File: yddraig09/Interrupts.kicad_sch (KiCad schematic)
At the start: 13 parts, among them U18 74LS32, U19 74LS574, U20 74LS32, U21 74LS11, U22 74LS147, U23 74LS540

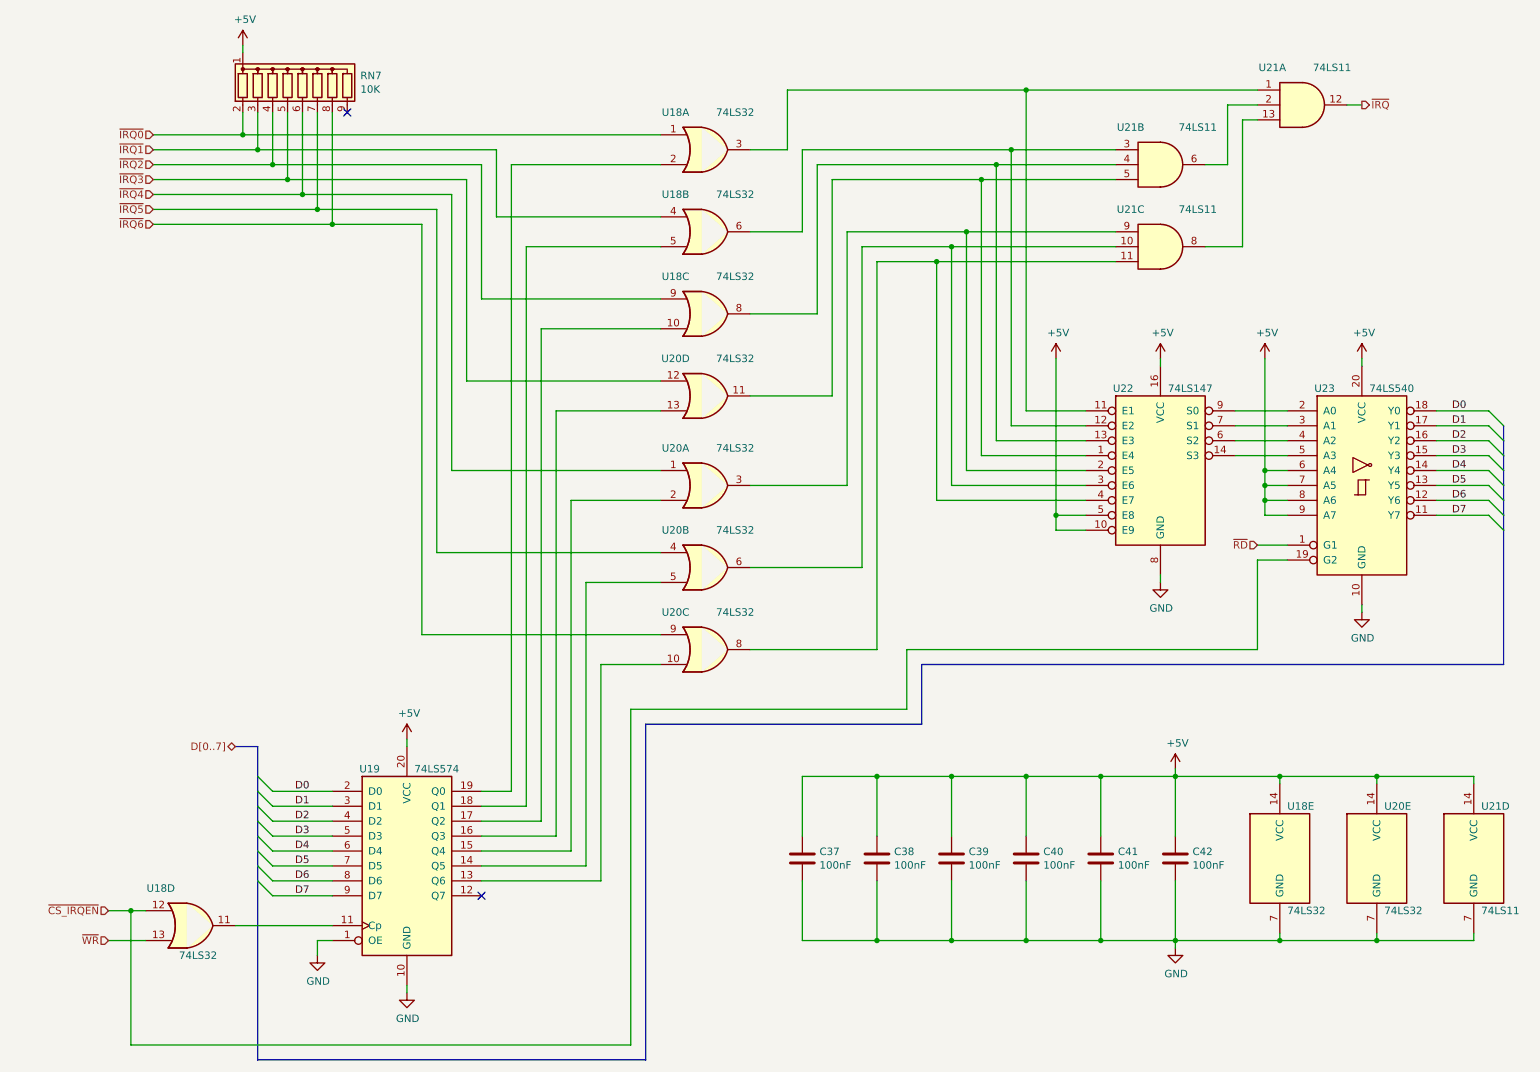
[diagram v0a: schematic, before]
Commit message: Finished changes to 6809 schematics
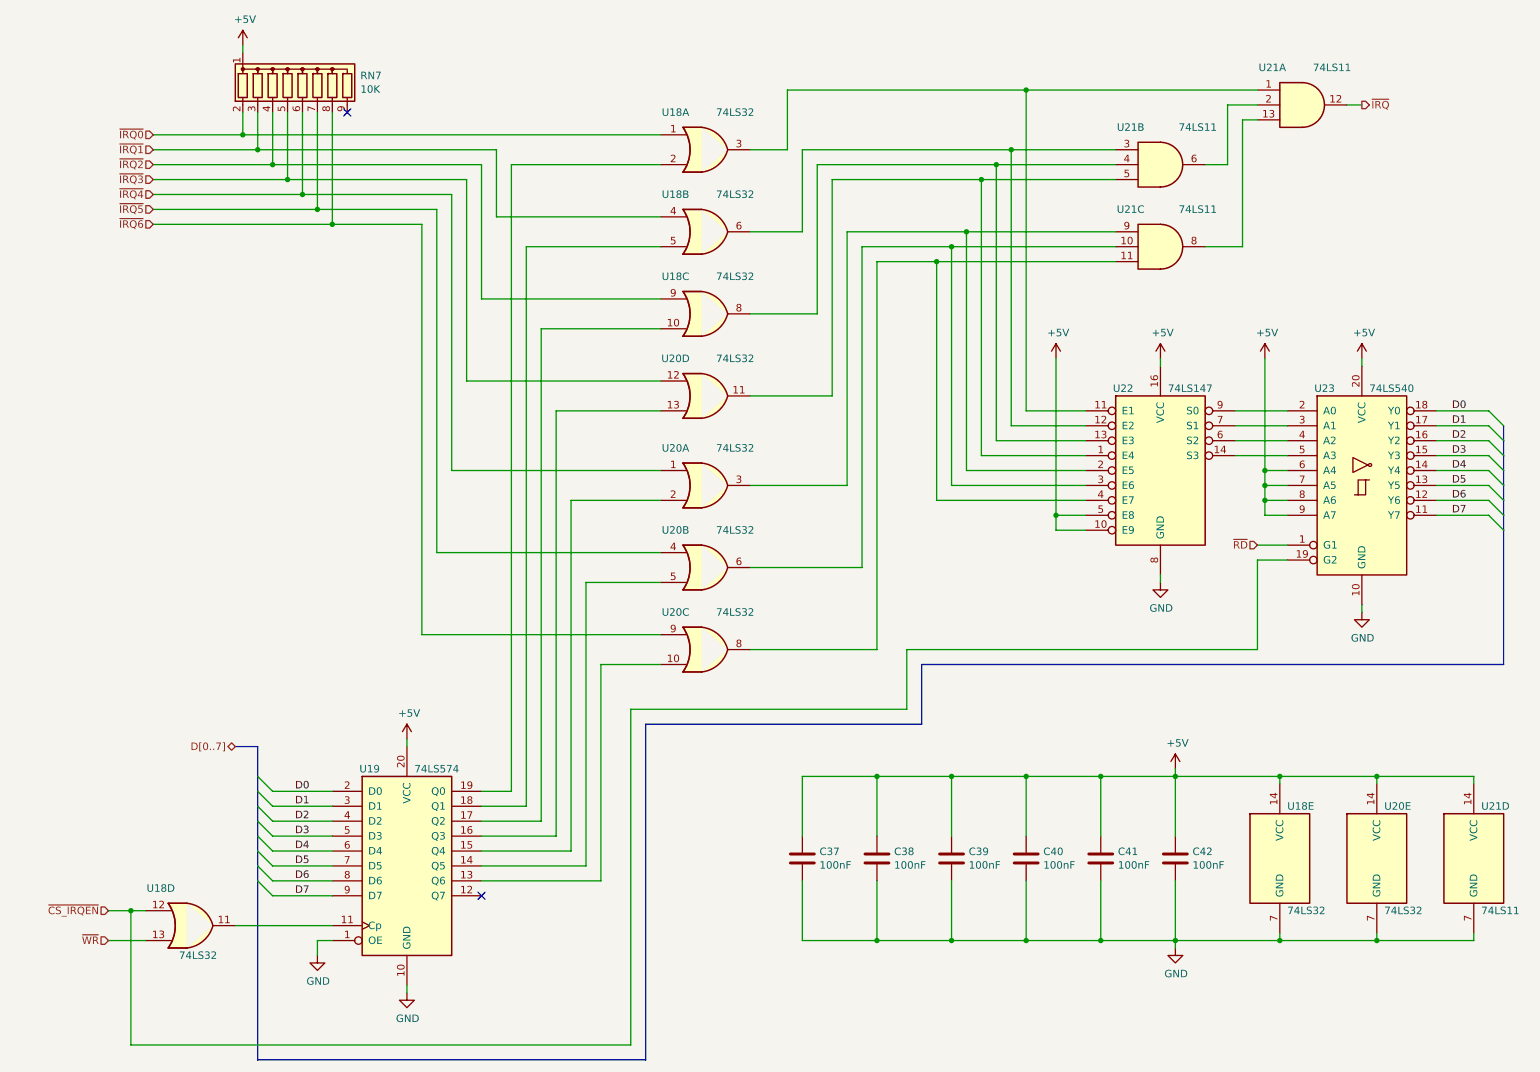
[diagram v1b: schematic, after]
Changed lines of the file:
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@@
 			)
 		)
-		(property "Description" ""
+		(property "Description" "Triple 3-input AND"
 			(at 241.3 30.48 0)
 			(effects
@@
 			)
 		)
-		(property "Description" ""
+		(property "Description" "Triple 3-input AND"
 			(at 217.17 40.64 0)
 			(effects
@@
 			)
 		)
-		(property "Description" ""
+		(property "Description" "Triple 3-input AND"
 			(at 217.17 54.61 0)
 			(effects
@@
 			)
 		)
-		(property "Description" ""
+		(property "Description" "Triple 3-input AND"
 			(at 270.51 158.75 0)
 			(effects
@@
 			)
 		)
-		(property "Description" ""
+		(property "Description" "Quad 2-input OR"
 			(at 139.7 38.1 0)
 			(effects
@@
 			)
 		)
-		(property "Description" ""
+		(property "Description" "Quad 2-input OR"
 			(at 139.7 52.07 0)
 			(effects
@@
 			)
 		)
-		(property "Description" ""
+		(property "Description" "Quad 2-input OR"
 			(at 139.7 66.04 0)
 			(effects
@@
 			)
 		)
-		(property "Description" ""
+		(property "Description" "Quad 2-input OR"
 			(at 139.7 80.01 0)
 			(effects
@@
 			)
 		)
-		(property "Description" ""
+		(property "Description" "Quad 2-input OR"
 			(at 254 158.75 0)
 			(effects
@@
 			)
 		)
-		(property "Description" ""
+		(property "Description" "Quad 2-input OR"
 			(at 139.7 95.25 0)
 			(effects
@@
 			)
 		)
-		(property "Description" ""
+		(property "Description" "Quad 2-input OR"
 			(at 139.7 109.22 0)
 			(effects
@@
 			)
 		)
-		(property "Description" ""
+		(property "Description" "Quad 2-input OR"
 			(at 139.7 123.19 0)
 			(effects
@@
 			)
 		)
-		(property "Description" ""
+		(property "Description" "Quad 2-input OR"
 			(at 52.07 170.18 0)
 			(effects
@@
 			)
 		)
-		(property "Description" ""
+		(property "Description" "Quad 2-input OR"
 			(at 237.49 158.75 0)
 			(effects
@@
 			)
 		)
-		(property "Description" ""
+		(property "Description" "8 resistor network, star topology, bussed resistors, small symbol"
 			(at 71.12 26.67 0)
 			(effects
@@
 			)
 		)
-		(property "Description" ""
+		(property "Description" "Priority Encoder, 10 to 4"
 			(at 217.17 92.71 0)
 			(effects
@@
 			)
 		)
-		(property "Description" ""
+		(property "Description" "8-bit Buffer/Line driver Inverter, 3-state outputs"
 			(at 251.46 95.25 0)
 			(effects
@@
 			)
 		)
-		(property "Description" ""
+		(property "Description" "8-bit Register, 3-state outputs"
 			(at 88.9 160.02 0)
 			(effects
@@
 			)
 		)
-		(property "Description" ""
+		(property "Description" "Power symbol creates a global label with name \"GND\" , ground"
 			(at 88.9 181.61 0)
 			(effects
@@
 			)
 		)
-		(property "Description" ""
+		(property "Description" "Power symbol creates a global label with name \"GND\" , ground"
 			(at 73.66 175.26 0)
 			(effects
@@
 			)
 		)
-		(property "Description" ""
+		(property "Description" "Power symbol creates a global label with name \"+5V\""
 			(at 60.96 20.32 0)
 			(effects
@@
 			)
 		)
-		(property "Description" ""
+		(property "Description" "Power symbol creates a global label with name \"+5V\""
 			(at 217.17 73.66 0)
 			(effects
@@
 			)
 		)
-		(property "Description" ""
+		(property "Description" "Power symbol creates a global label with name \"+5V\""
 			(at 251.46 73.66 0)
 			(effects
@@
 			)
 		)
-		(property "Description" ""
+		(property "Description" "Power symbol creates a global label with name \"GND\" , ground"
 			(at 217.17 111.76 0)
 			(effects
@@
 			)
 		)
-		(property "Description" ""
+		(property "Description" "Power symbol creates a global label with name \"GND\" , ground"
 			(at 251.46 116.84 0)
 			(effects
@@
 			)
 		)
-		(property "Description" ""
+		(property "Description" "Power symbol creates a global label with name \"+5V\""
 			(at 234.95 73.66 0)
 			(effects
@@
 			)
 		)
-		(property "Description" ""
+		(property "Description" "Power symbol creates a global label with name \"+5V\""
 			(at 199.39 73.66 0)
 			(effects
@@
 			)
 		)
-		(property "Description" ""
+		(property "Description" "Power symbol creates a global label with name \"+5V\""
 			(at 88.9 138.43 0)
 			(effects
@@
 			)
 		)
-		(property "Description" ""
+		(property "Description" "Power symbol creates a global label with name \"GND\" , ground"
 			(at 219.71 173.99 0)
 			(effects
@@
 			)
 		)
-		(property "Description" ""
+		(property "Description" "Power symbol creates a global label with name \"+5V\""
 			(at 219.71 143.51 0)
 			(effects
@@
 			)
 		)
-		(property "Description" ""
+		(property "Description" "Unpolarized capacitor"
 			(at 156.21 158.75 0)
 			(effects
@@
 			)
 		)
-		(property "Description" ""
+		(property "Description" "Unpolarized capacitor"
 			(at 168.91 158.75 0)
 			(effects
@@
 			)
 		)
-		(property "Description" ""
+		(property "Description" "Unpolarized capacitor"
 			(at 181.61 158.75 0)
 			(effects
@@
 			)
 		)
-		(property "Description" ""
+		(property "Description" "Unpolarized capacitor"
 			(at 194.31 158.75 0)
 			(effects
@@
 			)
 		)
-		(property "Description" ""
+		(property "Description" "Unpolarized capacitor"
 			(at 207.01 158.75 0)
 			(effects
@@
 			)
 		)
-		(property "Description" ""
+		(property "Description" "Unpolarized capacitor"
 			(at 219.71 158.75 0)
 			(effects

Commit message: 6809 board changes
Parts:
- renumbered RN7 to RN4
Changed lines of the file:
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@@
 		(on_board yes)
 		(dnp no)
-		(property "Reference" "RN7"
+		(property "Reference" "RN4"
 			(at 80.9752 25.5016 0)
 			(effects
@@
 			(project "yddraig09"
 				(path "/3cf18d79-3df5-467d-a147-795d8b124c26/00000000-0000-0000-0000-00006162d433"
-					(reference "RN7")
+					(reference "RN4")
 					(unit 1)
 				)
@@
 		(on_board yes)
 		(dnp no)
-		(property "Reference" "#PWR097"
+		(property "Reference" "#PWR093"
 			(at 88.9 187.96 0)
 			(effects
@@
 			(project "yddraig09"
 				(path "/3cf18d79-3df5-467d-a147-795d8b124c26/00000000-0000-0000-0000-00006162d433"
-					(reference "#PWR097")
+					(reference "#PWR093")
 					(unit 1)
 				)
@@
 		(on_board yes)
 		(dnp no)
-		(property "Reference" "#PWR095"
+		(property "Reference" "#PWR091"
 			(at 73.66 181.61 0)
 			(effects
@@
 			(project "yddraig09"
 				(path "/3cf18d79-3df5-467d-a147-795d8b124c26/00000000-0000-0000-0000-00006162d433"
-					(reference "#PWR095")
+					(reference "#PWR091")
 					(unit 1)
 				)
@@
 		(on_board yes)
 		(dnp no)
-		(property "Reference" "#PWR094"
+		(property "Reference" "#PWR090"
 			(at 60.96 24.13 0)
 			(effects
@@
 			(project "yddraig09"
 				(path "/3cf18d79-3df5-467d-a147-795d8b124c26/00000000-0000-0000-0000-00006162d433"
-					(reference "#PWR094")
+					(reference "#PWR090")
 					(unit 1)
 				)
@@
 		(on_board yes)
 		(dnp no)
-		(property "Reference" "#PWR099"
+		(property "Reference" "#PWR095"
 			(at 217.17 77.47 0)
 			(effects
@@
 			(project "yddraig09"
 				(path "/3cf18d79-3df5-467d-a147-795d8b124c26/00000000-0000-0000-0000-00006162d433"
-					(reference "#PWR099")
+					(reference "#PWR095")
 					(unit 1)
 				)
@@
 		(on_board yes)
 		(dnp no)
-		(property "Reference" "#PWR0104"
+		(property "Reference" "#PWR0100"
 			(at 251.46 77.47 0)
 			(effects
@@
 			(project "yddraig09"
 				(path "/3cf18d79-3df5-467d-a147-795d8b124c26/00000000-0000-0000-0000-00006162d433"
-					(reference "#PWR0104")
+					(reference "#PWR0100")
 					(unit 1)
 				)
@@
 		(on_board yes)
 		(dnp no)
-		(property "Reference" "#PWR0100"
+		(property "Reference" "#PWR096"
 			(at 217.17 118.11 0)
 			(effects
@@
 			(project "yddraig09"
 				(path "/3cf18d79-3df5-467d-a147-795d8b124c26/00000000-0000-0000-0000-00006162d433"
-					(reference "#PWR0100")
+					(reference "#PWR096")
 					(unit 1)
 				)
@@
 		(on_board yes)
 		(dnp no)
-		(property "Reference" "#PWR0105"
+		(property "Reference" "#PWR0101"
 			(at 251.46 123.19 0)
 			(effects
@@
 			(project "yddraig09"
 				(path "/3cf18d79-3df5-467d-a147-795d8b124c26/00000000-0000-0000-0000-00006162d433"
-					(reference "#PWR0105")
+					(reference "#PWR0101")
 					(unit 1)
 				)
@@
 		(on_board yes)
 		(dnp no)
-		(property "Reference" "#PWR0103"
+		(property "Reference" "#PWR099"
 			(at 234.95 77.47 0)
 			(effects
@@
 			(project "yddraig09"
 				(path "/3cf18d79-3df5-467d-a147-795d8b124c26/00000000-0000-0000-0000-00006162d433"
-					(reference "#PWR0103")
+					(reference "#PWR099")
 					(unit 1)
 				)
@@
 		(on_board yes)
 		(dnp no)
-		(property "Reference" "#PWR098"
+		(property "Reference" "#PWR094"
 			(at 199.39 77.47 0)
 			(effects
@@
 			(project "yddraig09"
 				(path "/3cf18d79-3df5-467d-a147-795d8b124c26/00000000-0000-0000-0000-00006162d433"
-					(reference "#PWR098")
+					(reference "#PWR094")
 					(unit 1)
 				)
@@
 		(on_board yes)
 		(dnp no)
-		(property "Reference" "#PWR096"
+		(property "Reference" "#PWR092"
 			(at 88.9 142.24 0)
 			(effects
@@
 			(project "yddraig09"
 				(path "/3cf18d79-3df5-467d-a147-795d8b124c26/00000000-0000-0000-0000-00006162d433"
-					(reference "#PWR096")
+					(reference "#PWR092")
 					(unit 1)
 				)
@@
 		(on_board yes)
 		(dnp no)
-		(property "Reference" "#PWR0102"
+		(property "Reference" "#PWR098"
 			(at 219.71 180.34 0)
 			(effects
@@
 			(project "yddraig09"
 				(path "/3cf18d79-3df5-467d-a147-795d8b124c26/00000000-0000-0000-0000-00006162d433"
-					(reference "#PWR0102")
+					(reference "#PWR098")
 					(unit 1)
 				)
@@
 		(on_board yes)
 		(dnp no)
-		(property "Reference" "#PWR0101"
+		(property "Reference" "#PWR097"
 			(at 219.71 147.32 0)
 			(effects
@@
 			(project "yddraig09"
 				(path "/3cf18d79-3df5-467d-a147-795d8b124c26/00000000-0000-0000-0000-00006162d433"
-					(reference "#PWR0101")
-					(unit 1)
-				)
+					(reference "#PWR097")
+					(unit 1)
+				)

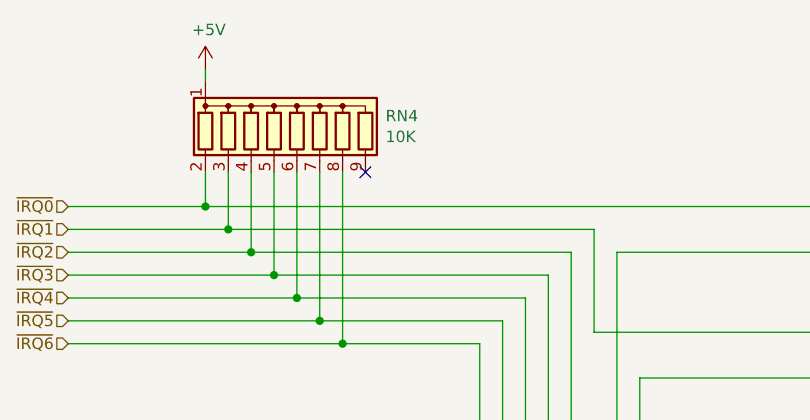
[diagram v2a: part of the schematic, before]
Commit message: Changed RTC
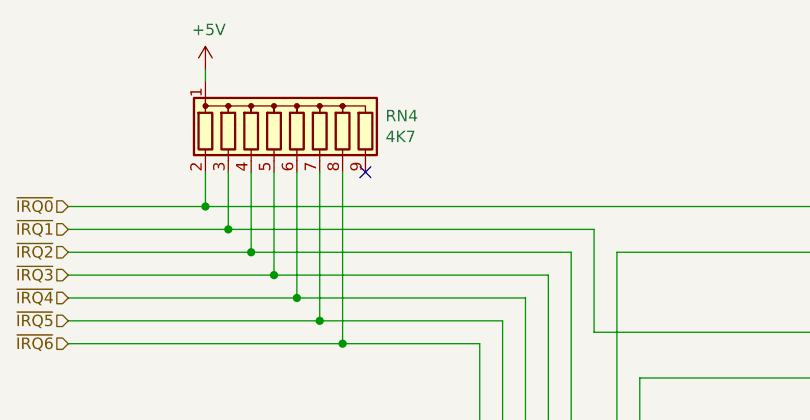
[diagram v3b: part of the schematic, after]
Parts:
- RN4: value 10K -> 4K7
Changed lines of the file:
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@@
 			)
 		)
-		(property "Value" "10K"
+		(property "Value" "4K7"
 			(at 80.9752 27.813 0)
 			(effects
